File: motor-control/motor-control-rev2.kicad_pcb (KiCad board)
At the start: 2 copper layers, 155.7 x 66 mm, 80 parts, among them P1 CONN_02X12, P2 to_motor_phase_1, P3 to_motor_phase_2, P4 to_motor_phase_3, P5 CONN_01X01, P6 CONN_01X01, P7 CONN_01X04, Q1 csd19505kcs, Q10 csd19505kcs, Q11 csd19505kcs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

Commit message: Redid board edge, increase copper&mask plane dist
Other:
- board size 155.7 x 66 mm -> 122.3 x 65.9 mm
- net class Default: clearance 0.18 -> 0.1524; trace_width 0.25 -> 0.1524
- rule trace_clearance: 0.18 -> 0.1524
- rule trace_min: 0.18 -> 0.1524
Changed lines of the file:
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@@
     (area 41.530199 20.5104 197.331401 92.527833)
     (thickness 1.6)
-    (drawings 5)
+    (drawings 7)
     (tracks 1227)
     (zones 0)
@@
     (0 F.Cu signal)
     (31 B.Cu signal)
-    (32 B.Adhes user)
-    (33 F.Adhes user)
+    (32 B.Adhes user hide)
+    (33 F.Adhes user hide)
     (34 B.Paste user)
-    (35 F.Paste user)
-    (36 B.SilkS user)
-    (37 F.SilkS user)
-    (38 B.Mask user)
-    (39 F.Mask user)
-    (40 Dwgs.User user)
-    (41 Cmts.User user)
-    (42 Eco1.User user)
-    (43 Eco2.User user)
+    (35 F.Paste user hide)
+    (36 B.SilkS user hide)
+    (37 F.SilkS user hide)
+    (38 B.Mask user hide)
+    (39 F.Mask user hide)
+    (40 Dwgs.User user hide)
+    (41 Cmts.User user hide)
+    (42 Eco1.User user hide)
+    (43 Eco2.User user hide)
     (44 Edge.Cuts user)
-    (45 Margin user)
-    (46 B.CrtYd user)
-    (47 F.CrtYd user)
-    (48 B.Fab user)
-    (49 F.Fab user)
+    (45 Margin user hide)
+    (46 B.CrtYd user hide)
+    (47 F.CrtYd user hide)
+    (48 B.Fab user hide)
+    (49 F.Fab user hide)
   )
   (setup
-    (last_trace_width 0.25)
+    (last_trace_width 0.1524)
     (user_trace_width 0.18)
     (user_trace_width 0.3)
@@
     (user_trace_width 2)
     (user_trace_width 6)
-    (trace_clearance 0.18)
+    (trace_clearance 0.1524)
     (zone_clearance 0.508)
     (zone_45_only no)
-    (trace_min 0.18)
+    (trace_min 0.1524)
     (segment_width 0.2)
     (edge_width 0.15)
@@
   (net 72 "Net-(P7-Pad4)")
   (net_class Default "This is the default net class."
-    (clearance 0.18)
-    (trace_width 0.25)
+    (clearance 0.1524)
+    (trace_width 0.1524)
     (via_dia 0.6)
     (via_drill 0.4)
@@
     )
   )
-  (gr_line (start 41.9735 89.5096) (end 41.9862 89.4207) (layer Edge.Cuts) (width 0.15))
-  (gr_line (start 41.9227 23.7744) (end 41.9735 89.5096) (layer Edge.Cuts) (width 0.15))
-  (gr_line (start 196.9389 23.5585) (end 41.6052 23.5585) (layer Edge.Cuts) (width 0.15))
-  (gr_line (start 196.9389 89.2048) (end 196.9389 23.5585) (layer Edge.Cuts) (width 0.15))
-  (gr_line (start 41.7068 89.4207) (end 197.2564 89.4207) (layer Edge.Cuts) (width 0.15))
+  (gr_line (start 74.549 23.495) (end 74.549 23.622) (layer Edge.Cuts) (width 0.15))
+  (gr_line (start 196.85 23.495) (end 74.549 23.495) (layer Edge.Cuts) (width 0.15))
+  (gr_line (start 196.85 89.408) (end 196.85 23.495) (layer Edge.Cuts) (width 0.15))
+  (gr_line (start 196.85 89.408) (end 196.85 89.408) (layer Edge.Cuts) (width 0.15))
+  (gr_line (start 74.549 89.408) (end 196.85 89.408) (layer Edge.Cuts) (width 0.15))
+  (gr_line (start 74.549 89.408) (end 74.549 23.749) (layer Edge.Cuts) (width 0.15))
+  (gr_line (start 74.549 23.749) (end 74.549 23.622) (layer Edge.Cuts) (width 0.15))
   (segment (start 93.8972 48.32462) (end 92.951479 47.378899) (width 1) (layer F.Cu) (net 1))
   (segment (start 92.951479 47.378899) (end 92.65148 47.0789) (width 1) (layer F.Cu) (net 1))
@@
     (polygon
       (pts
-        (xy 107.8357 24.7904) (xy 107.8357 43.3197) (xy 111.506 46.99) (xy 117.5512 46.99) (xy 119.0244 45.5168)
-        (xy 119.0244 39.5605) (xy 128.3716 30.2133) (xy 128.3716 26.5049) (xy 126.2253 24.3586) (xy 108.2675 24.3586)
+        (xy 107.8357 24.7904) (xy 107.8357 43.3197) (xy 111.506 46.99) (xy 117.5512 46.99) (xy 118.745 45.466)
+        (xy 118.745 39.497) (xy 128.27 29.972) (xy 128.3716 26.5049) (xy 126.2253 24.3586) (xy 108.2675 24.3586)
       )
     )
@@
     (polygon
       (pts
-        (xy 156.50718 86.94928) (xy 156.50718 80.3021) (xy 162.56254 74.24674) (xy 166.74084 74.24674) (xy 169.86504 77.37094)
-        (xy 174.1043 77.37094) (xy 178.07178 81.33842) (xy 181.64556 81.33842) (xy 183.47944 79.50454) (xy 183.47944 70.66534)
+        (xy 156.50718 86.94928) (xy 156.845 80.518) (xy 162.56 74.549) (xy 166.7383 74.549) (xy 169.672 77.724)
+        (xy 174.117 77.724) (xy 177.927 81.534) (xy 181.737 81.534) (xy 184.023 79.629) (xy 184.023 70.358)
         (xy 188.80328 65.3415) (xy 188.80328 62.2681) (xy 190.00724 61.06414) (xy 195.8975 61.06414) (xy 196.40804 61.57468)
         (xy 196.40804 86.05774) (xy 193.5353 88.93048) (xy 158.4579 88.93048) (xy 156.49956 86.97214)
@@
     )
   )
-  (zone (net 1) (net_name +batt) (layer B.Mask) (hatch edge 0.508)
+  (zone (net 0) (net_name "") (layer B.Mask) (hatch edge 0.508)
     (connect_pads yes (clearance 0.508))
     (min_thickness 0.254)
@@
     (polygon
       (pts
-        (xy 183.47944 70.66534) (xy 183.47944 79.44104) (xy 181.62778 81.2927) (xy 178.06924 81.2927) (xy 174.12208 77.34554)
-        (xy 169.88536 77.34554) (xy 166.74846 74.20864) (xy 162.54984 74.20864) (xy 156.47416 80.28432) (xy 156.47416 87.0077)
+        (xy 183.769 70.739) (xy 183.769 79.5147) (xy 181.61 81.661) (xy 178.05146 81.661) (xy 174.117 77.724)
+        (xy 169.545 77.724) (xy 166.41572 74.549) (xy 162.55238 74.549) (xy 156.718 80.391) (xy 156.718 87.11438)
         (xy 158.4325 88.96604) (xy 193.53276 88.96604) (xy 196.4436 86.0552) (xy 196.4436 76.7461) (xy 194.27444 74.57694)
         (xy 192.8241 74.57694) (xy 192.4177 74.17054) (xy 192.4177 69.1261) (xy 191.63538 68.34378) (xy 191.63538 67.564)
@@
         (xy 194.63004 74.9046) (xy 196.4436 76.71816) (xy 196.4436 61.56198) (xy 195.88734 61.00572) (xy 195.15836 61.00572)
         (xy 194.59194 61.57214) (xy 194.59194 61.8109) (xy 192.76314 61.8109) (xy 192.20688 61.25464) (xy 192.01384 61.25464)
-        (xy 189.92596 61.25464) (xy 188.94552 62.23508) (xy 188.94552 65.2907) (xy 183.60898 70.62724) (xy 183.51754 70.62724)
+        (xy 189.92596 61.25464) (xy 188.94552 62.23508) (xy 188.94552 65.2907) (xy 183.769 70.485) (xy 183.67756 70.485)
       )
     )
   )
-  (zone (net 1) (net_name +batt) (layer B.Mask) (hatch edge 0.508)
+  (zone (net 0) (net_name "") (layer B.Mask) (hatch edge 0.508)
     (connect_pads yes (clearance 0.508))
     (min_thickness 0.254)
@@
     )
   )
-  (zone (net 1) (net_name +batt) (layer B.Mask) (hatch edge 0.508)
+  (zone (net 0) (net_name "") (layer B.Mask) (hatch edge 0.508)
     (connect_pads yes (clearance 0.508))
     (min_thickness 0.254)
@@
     )
   )
-  (zone (net 1) (net_name +batt) (layer B.Mask) (hatch edge 0.508)
+  (zone (net 0) (net_name "") (layer B.Mask) (hatch edge 0.508)
     (connect_pads yes (clearance 0.508))
     (min_thickness 0.254)
@@
     )
   )
-  (zone (net 1) (net_name +batt) (layer B.Mask) (hatch edge 0.508)
+  (zone (net 0) (net_name "") (layer B.Mask) (hatch edge 0.508)
     (connect_pads yes (clearance 0.508))
     (min_thickness 0.254)
@@
     )
   )
-  (zone (net 1) (net_name +batt) (layer B.Mask) (hatch edge 0.508)
+  (zone (net 0) (net_name "") (layer B.Mask) (hatch edge 0.508)
     (connect_pads yes (clearance 0.508))
     (min_thickness 0.254)
@@
     )
   )
-  (zone (net 1) (net_name +batt) (layer B.Mask) (hatch edge 0.508)
+  (zone (net 0) (net_name "") (layer B.Mask) (hatch edge 0.508)
     (connect_pads yes (clearance 0.508))
     (min_thickness 0.254)

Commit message: Almost! Added digital gnd, & connected some gnds
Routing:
- net GND: track 71.8 -> 107.1 mm, vias 0 -> 5
- added copper zone on F.Cu, net GND
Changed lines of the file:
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@@
   (general
     (links 228)
-    (no_connects 37)
-    (area 41.530199 20.5104 197.331401 92.527833)
+    (no_connects 24)
+    (area 74.473999 23.419999 196.925001 89.483001)
     (thickness 1.6)
     (drawings 7)
-    (tracks 1227)
+    (tracks 1263)
     (zones 0)
     (modules 80)
@@
     (36 B.SilkS user hide)
     (37 F.SilkS user hide)
-    (38 B.Mask user hide)
-    (39 F.Mask user hide)
+    (38 B.Mask user)
+    (39 F.Mask user)
     (40 Dwgs.User user hide)
     (41 Cmts.User user hide)
@@
   (segment (start 93.9038 50.9778) (end 94.6785 51.7525) (width 1) (layer F.Cu) (net 1))
   (segment (start 93.9038 50.6984) (end 93.9038 50.9778) (width 1) (layer F.Cu) (net 1))
+  (segment (start 112.014 54.483) (end 107.95 58.547) (width 0.1524) (layer B.Cu) (net 2))
+  (segment (start 107.95 58.547) (end 107.95 60.579) (width 0.1524) (layer B.Cu) (net 2))
+  (segment (start 110.7567 54.737) (end 111.76 54.737) (width 0.1524) (layer F.Cu) (net 2))
+  (segment (start 111.76 54.737) (end 112.014 54.483) (width 0.1524) (layer F.Cu) (net 2))
+  (via (at 112.014 54.483) (size 0.6) (drill 0.4) (layers F.Cu B.Cu) (net 2))
+  (segment (start 100.4062 72.6374) (end 100.4062 73.5838) (width 0.1524) (layer F.Cu) (net 2))
+  (segment (start 100.4062 73.5838) (end 99.822 74.168) (width 0.1524) (layer F.Cu) (net 2))
+  (via (at 99.822 74.168) (size 0.6) (drill 0.4) (layers F.Cu B.Cu) (net 2))
+  (segment (start 102.3239 70.8787) (end 103.1013 70.8787) (width 0.1524) (layer F.Cu) (net 2))
+  (segment (start 103.1013 70.8787) (end 104.1527 69.8273) (width 0.1524) (layer F.Cu) (net 2))
+  (segment (start 104.1527 69.8273) (end 104.1527 69.4737) (width 0.1524) (layer F.Cu) (net 2))
+  (segment (start 104.1527 69.4737) (end 104.1527 68.8213) (width 0.1524) (layer F.Cu) (net 2))
+  (segment (start 100.4062 72.6374) (end 100.5312 72.6374) (width 0.1524) (layer F.Cu) (net 2))
+  (segment (start 100.5312 72.6374) (end 102.2899 70.8787) (width 0.1524) (layer F.Cu) (net 2))
+  (segment (start 102.2899 70.8787) (end 102.3239 70.8787) (width 0.1524) (layer F.Cu) (net 2))
+  (segment (start 89.22 57.9374) (end 88.6206 57.9374) (width 0.1524) (layer F.Cu) (net 2))
+  (segment (start 88.6206 57.9374) (end 86.868 59.69) (width 0.1524) (layer F.Cu) (net 2))
+  (via (at 86.868 59.69) (size 0.6) (drill 0.4) (layers F.Cu B.Cu) (net 2))
+  (segment (start 89.2495 62.1157) (end 89.2495 61.9519) (width 0.1524) (layer F.Cu) (net 2))
+  (segment (start 89.2495 61.9519) (end 90.9828 60.2186) (width 0.1524) (layer F.Cu) (net 2))
+  (segment (start 90.9828 60.2186) (end 90.9828 59.9186) (width 0.1524) (layer F.Cu) (net 2))
+  (segment (start 89.22 57.9374) (end 89.22 58.2374) (width 0.1524) (layer F.Cu) (net 2))
+  (segment (start 89.22 58.2374) (end 90.9012 59.9186) (width 0.1524) (layer F.Cu) (net 2))
+  (segment (start 90.9012 59.9186) (end 90.9828 59.9186) (width 0.1524) (layer F.Cu) (net 2))
+  (segment (start 110.236 64.135) (end 109.4867 64.8843) (width 0.1524) (layer F.Cu) (net 2))
+  (segment (start 109.4867 64.8843) (end 108.5723 64.8843) (width 0.1524) (layer F.Cu) (net 2))
+  (segment (start 108.839 61.087) (end 110.236 62.484) (width 0.1524) (layer B.Cu) (net 2))
+  (segment (start 110.236 62.484) (end 110.236 64.135) (width 0.1524) (layer B.Cu) (net 2))
+  (via (at 110.236 64.135) (size 0.6) (drill 0.4) (layers F.Cu B.Cu) (net 2))
+  (segment (start 108.458 61.087) (end 108.839 61.087) (width 0.1524) (layer B.Cu) (net 2))
+  (segment (start 107.95 60.579) (end 108.458 61.087) (width 0.1524) (layer B.Cu) (net 2))
+  (segment (start 106.9357 60.7499) (end 107.7791 60.7499) (width 0.1524) (layer F.Cu) (net 2))
+  (segment (start 107.7791 60.7499) (end 107.95 60.579) (width 0.1524) (layer F.Cu) (net 2))
+  (via (at 107.95 60.579) (size 0.6) (drill 0.4) (layers F.Cu B.Cu) (net 2))
+  (segment (start 106.9357 60.7499) (end 106.9357 59.1999) (width 0.1524) (layer F.Cu) (net 2))
+  (segment (start 106.9357 59.1999) (end 106.6857 58.9499) (width 0.1524) (layer F.Cu) (net 2))
   (segment (start 149.235299 48.797401) (end 149.565301 48.467399) (width 0.3) (layer F.Cu) (net 2))
   (segment (start 142.8344 48.4378) (end 147.397298 48.4378) (width 0.3) (layer F.Cu) (net 2))
@@
       )
     )
+  )
+  (zone (net 0) (net_name "") (layer B.Mask) (hatch edge 0.508)
+    (connect_pads yes (clearance 0.508))
+    (min_thickness 0.254)
+    (fill yes (arc_segments 16) (thermal_gap 0.508) (thermal_bridge_width 0.508))
+    (polygon
+      (pts
+        (xy 136.652 26.543) (xy 136.652 30.099) (xy 138.938 32.385) (xy 139.7 32.385) (xy 142.113 29.972)
+        (xy 142.113 26.035) (xy 144.272 26.035) (xy 144.272 30.861) (xy 140.462 34.671) (xy 140.462 36.83)
+        (xy 138.684 36.83) (xy 138.303 36.449) (xy 138.303 34.671) (xy 134.493 30.861) (xy 134.493 26.67)
+        (xy 134.62 26.543)
+      )
+    )
+  )
+  (zone (net 2) (net_name GND) (layer B.Cu) (hatch edge 0.508)
+    (connect_pads (clearance 0.508))
+    (min_thickness 0.254)
+    (fill yes (arc_segments 16) (thermal_gap 0.508) (thermal_bridge_width 0.508))
+    (polygon
+      (pts
+        (xy 89.408 24.384) (xy 106.299 24.384) (xy 106.807 24.892) (xy 106.807 44.323) (xy 111.252 48.768)
+        (xy 119.888 48.768) (xy 122.682 51.562) (xy 123.825 52.705) (xy 125.095 52.705) (xy 125.095 53.467)
+        (xy 123.825 53.467) (xy 122.936 54.356) (xy 122.936 55.753) (xy 114.173 64.516) (xy 114.173 72.771)
+        (xy 115.316 73.914) (xy 115.316 74.422) (xy 115.062 74.676) (xy 107.188 74.676) (xy 106.68 75.184)
+        (xy 106.68 88.519) (xy 106.299 88.9) (xy 75.565 88.9) (xy 74.93 88.265) (xy 74.93 25.781)
+        (xy 76.327 24.384)
+      )
+    )
+  )
+  (zone (net 2) (net_name GND) (layer F.Cu) (hatch edge 0.508)
+    (connect_pads (clearance 0.508))
+    (min_thickness 0.254)
+    (fill yes (arc_segments 16) (thermal_gap 0.508) (thermal_bridge_width 0.508))
+    (polygon
+      (pts
+        (xy 82.931 24.384) (xy 106.299 24.384) (xy 106.807 24.892) (xy 106.807 37.973) (xy 112.903 44.069)
+        (xy 116.713 44.069) (xy 123.825 51.181) (xy 123.825 54.864) (xy 114.173 64.516) (xy 114.173 72.771)
+        (xy 115.316 73.914) (xy 115.316 74.422) (xy 115.062 74.676) (xy 107.188 74.676) (xy 106.68 75.184)
+        (xy 106.68 88.519) (xy 106.299 88.9) (xy 75.565 88.9) (xy 74.93 88.265) (xy 74.93 25.781)
+        (xy 76.327 24.384)
+      )
+    )

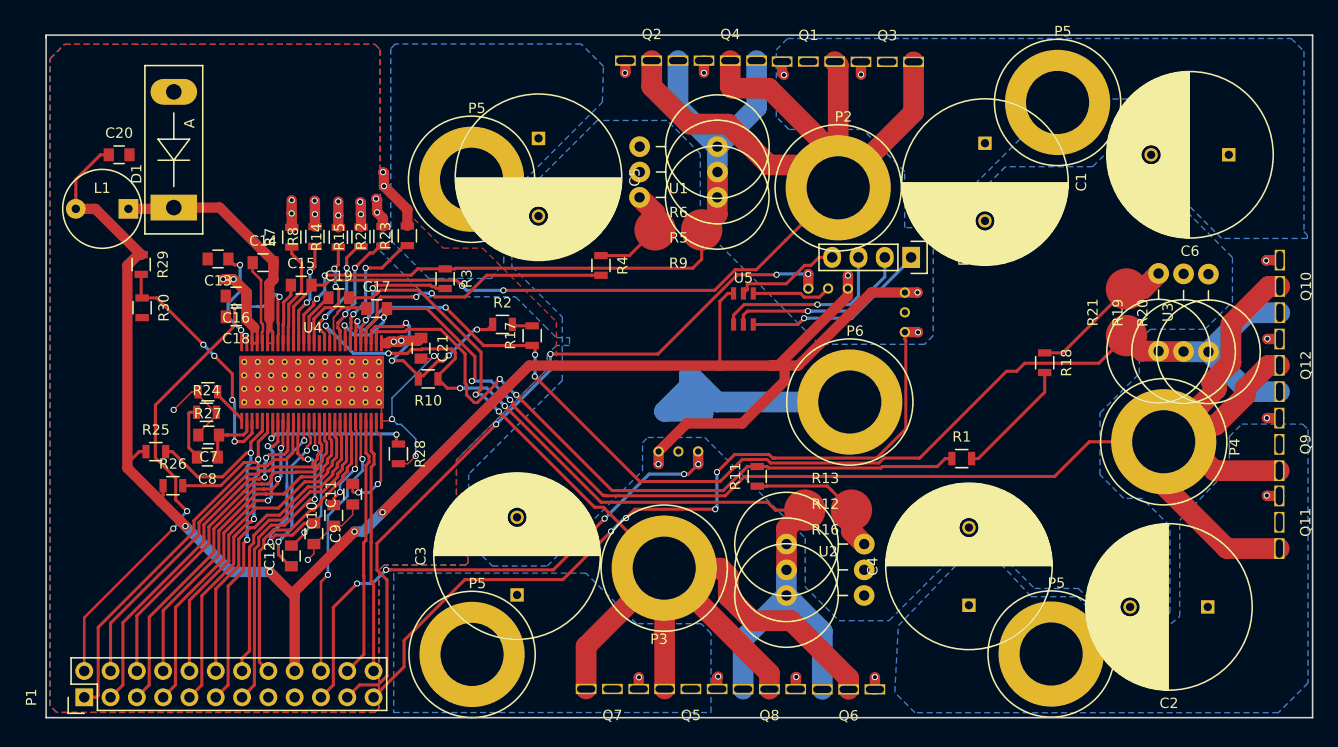
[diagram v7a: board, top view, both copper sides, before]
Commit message: Silkscreen round 1: oriented labels
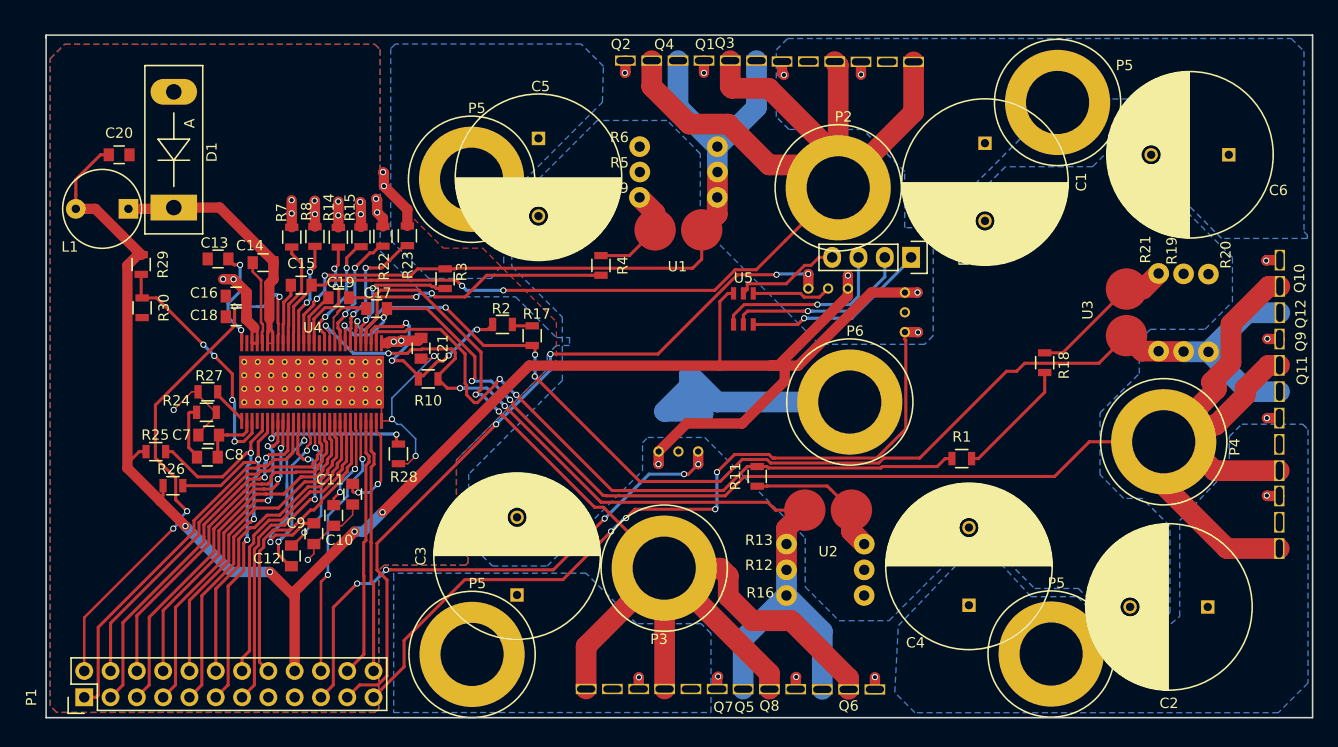
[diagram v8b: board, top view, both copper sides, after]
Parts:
- R12, R13, R16, R19, R20, R21, R5, R6, R9: footprint Resistors_ThroughHole:Resistor_Vertical_RM7.5mm -> p16261:Resistor_Vertical_RM7.5mm-edited
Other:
- board text added: "* means external jumper wire required"
